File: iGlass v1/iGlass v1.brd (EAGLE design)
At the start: 86.4 x 22.9 mm, 13 parts, among them J1 1040310811, U1 ABX00027

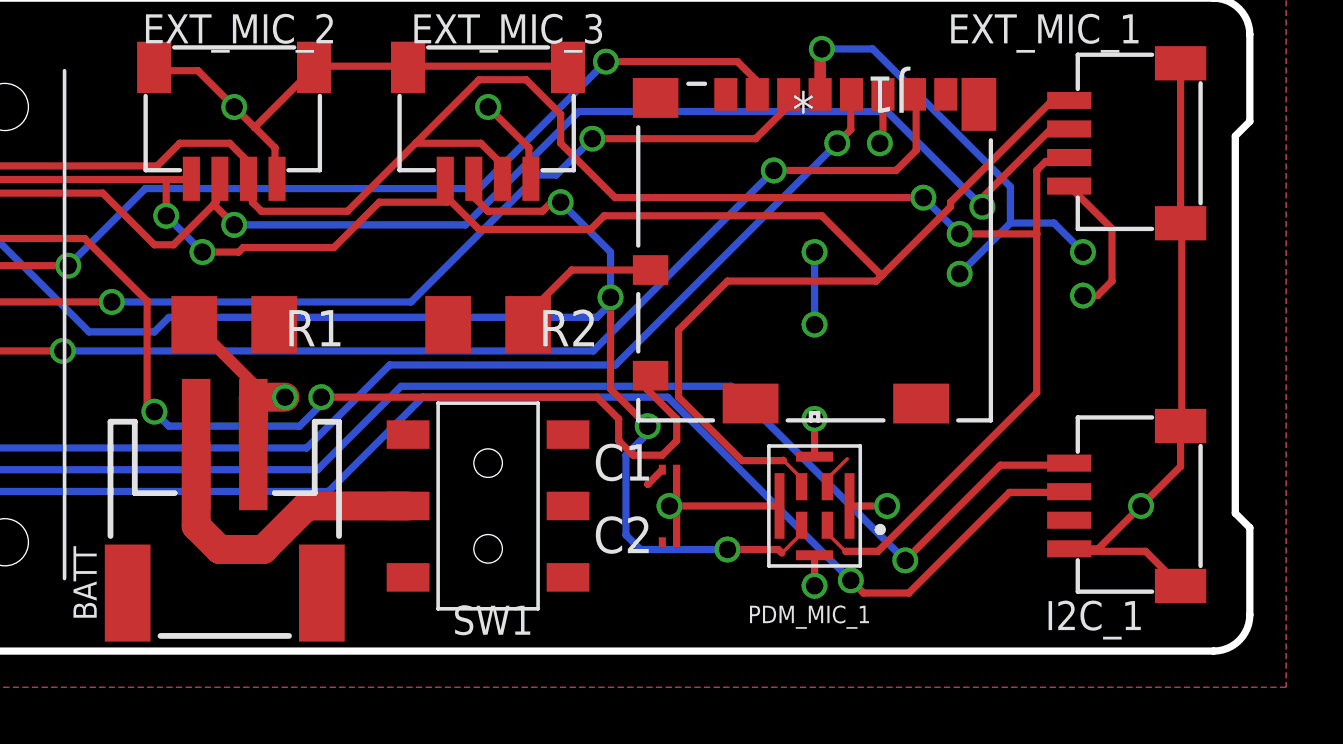
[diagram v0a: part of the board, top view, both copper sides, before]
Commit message: add pcb v2, v3
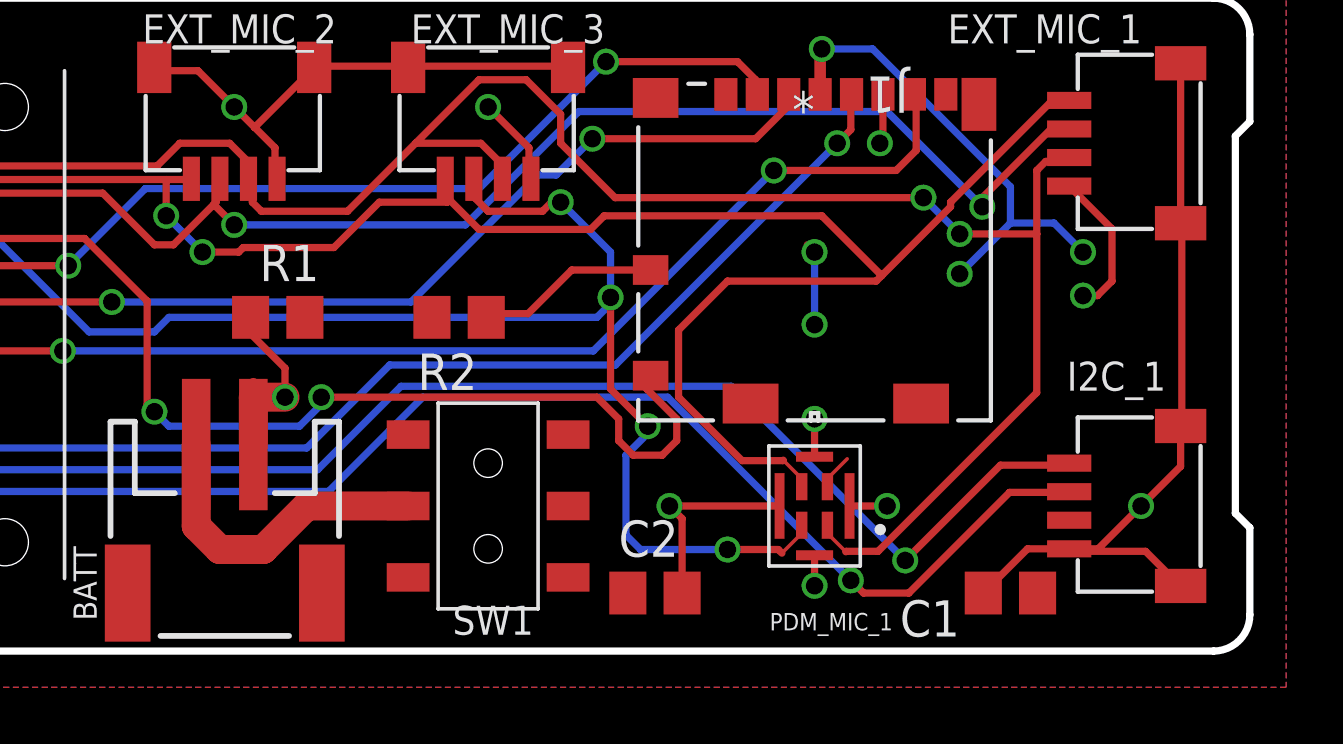
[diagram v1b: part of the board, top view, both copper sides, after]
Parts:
- C1, C2: device rcl:C0201 -> rcl:C0805
- R1, R2: device resistor:M1206 -> resistor:R0805
- moved C1 12.7 mm to (79.5, 3.56), turned to 180 degrees
- moved C2 1.85 mm to (67.1, 3.56)
- moved R1 1.55 mm to (53.8, 13.2)
- moved R2 1.05 mm to (60.2, 13.2), turned to 180 degrees
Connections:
- net N$3: now also R2.1; no longer R2.2
- net VCC: now also R2.2; no longer R2.1
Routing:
- net GND: track 73.4 -> 77.9 mm
- net N$3: track 5.31 -> 6.44 mm
- net VCC: track 21.6 -> 20.9 mm
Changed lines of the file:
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@@
 <attribute name="MF" value="STMicroelectronics" x="72.644" y="6.604" size="1.778" layer="27" rot="R180" display="off"/>
 <attribute name="MP" value="MP34DT01-M" x="72.644" y="6.604" size="1.778" layer="27" rot="R180" display="off"/>
-<attribute name="NAME" x="74.620390625" y="3.111240625" size="0.6096" layer="25" rot="R180"/>
+<attribute name="NAME" x="75.382390625" y="2.857240625" size="0.6096" layer="25" rot="R180"/>
 <attribute name="PACKAGE" value="None" x="72.644" y="6.604" size="1.778" layer="27" rot="R180" display="off"/>
 <attribute name="PRICE" value="None" x="72.644" y="6.604" size="1.778" layer="27" rot="R180" display="off"/>
@@
 <attribute name="PURCHASE-URL" value="https://pricing.snapeda.com/search/part/ABX00027/?ref=eda" x="24.384" y="12.954" size="1.778" layer="27" display="off"/>
 </element>
-<element name="C1" library="rcl" package="C0201" value="10uF" x="67.564" y="7.874" smashed="yes">
-<attribute name="NAME" x="64.897" y="7.493" size="1.27" layer="25"/>
-<attribute name="VALUE" x="67.183" y="8.255" size="1.27" layer="27"/>
-</element>
-<element name="C2" library="rcl" package="C0201" value="0.1uF" x="67.564" y="5.334" smashed="yes">
-<attribute name="NAME" x="64.897" y="4.953" size="1.27" layer="25"/>
-<attribute name="VALUE" x="65.405" y="3.175" size="1.27" layer="27"/>
-</element>
-<element name="R1" library="resistor" package="M1206" value="10K" x="52.324" y="12.954" smashed="yes">
-<attribute name="NAME" x="54.102" y="12.192" size="1.27" layer="25"/>
-<attribute name="VALUE" x="54.102" y="13.97" size="1.27" layer="27"/>
-</element>
 <element name="J1" library="micro_sd_slot" package="104031-0811_MOL" value="1040310811" x="72.644" y="15.494" smashed="yes" rot="R180">
 <attribute name="COPYRIGHT" value="Copyright (C) 2021 Ultra Librarian. All rights reserved." x="72.644" y="15.494" size="1.778" layer="27" rot="R180" display="off"/>
@@
 <attribute name="VALUE" x="74.3712" y="21.6408" size="1.27" layer="27" ratio="6" rot="SR180"/>
 </element>
-<element name="R2" library="resistor" package="M1206" value="100K" x="61.214" y="12.954" smashed="yes">
-<attribute name="NAME" x="62.992" y="12.192" size="1.27" layer="25"/>
-<attribute name="VALUE" x="60.96" y="14.224" size="1.27" layer="27"/>
-</element>
 <element name="EXT_MIC_3" library="smart-glasses" package="MICROBUILDER_JST_SH4" value="MICROBUILDER_STEMMA_I2C_QT" x="61.214" y="20.574" smashed="yes" rot="R180">
 <attribute name="NAME" x="65.306" y="23.818" size="1.016" layer="25" rot="R180"/>
 </element>
 <element name="I2C_1" library="smart-glasses" package="MICROBUILDER_JST_SH4" value="MICROBUILDER_STEMMA_I2C_QT" x="84.074" y="6.604" smashed="yes" rot="R90">
-<attribute name="NAME" x="80.714" y="2.258" size="1.016" layer="25"/>
+<attribute name="NAME" x="81.476" y="10.64" size="1.016" layer="25"/>
 </element>
 <element name="EXT_MIC_2" library="smart-glasses" package="MICROBUILDER_JST_SH4" value="MICROBUILDER_STEMMA_I2C_QT" x="52.324" y="20.574" smashed="yes" rot="R180">
@@
 <attribute name="NAME" x="46.6979" y="5.1943" size="0.8128" layer="25" ratio="18" rot="R270"/>
 <attribute name="VALUE" x="54.2163" y="3.7846" size="0.4064" layer="27" ratio="10" rot="R180"/>
+</element>
+<element name="R2" library="resistor" package="R0805" value="100K" x="60.198" y="13.208" smashed="yes" rot="R180">
+<attribute name="NAME" x="60.833" y="11.938" size="1.27" layer="25" rot="R180"/>
+<attribute name="VALUE" x="60.833" y="15.748" size="1.27" layer="27" rot="R180"/>
+</element>
+<element name="R1" library="resistor" package="R0805" value="10K" x="53.848" y="13.208" smashed="yes">
+<attribute name="NAME" x="53.213" y="14.478" size="1.27" layer="25"/>
+<attribute name="VALUE" x="53.213" y="10.668" size="1.27" layer="27"/>
+</element>
+<element name="C1" library="rcl" package="C0805" value="10uF" x="79.502" y="3.556" smashed="yes" rot="R180">
+<attribute name="NAME" x="77.724" y="3.302" size="1.27" layer="25" rot="R180"/>
+<attribute name="VALUE" x="80.772" y="6.096" size="1.27" layer="27" rot="R180"/>
+</element>
+<element name="C2" library="rcl" package="C0805" value="0.1uF" x="67.056" y="3.556" smashed="yes">
+<attribute name="NAME" x="65.786" y="4.826" size="1.27" layer="25"/>
+<attribute name="VALUE" x="70.104" y="2.032" size="1.27" layer="27" rot="R90"/>
 </element>
 </elements>
@@
 <contactref element="PDM_MIC_1" pad="5_3"/>
 <contactref element="PDM_MIC_1" pad="5_4"/>
-<contactref element="C2" pad="2"/>
-<contactref element="C1" pad="2"/>
-<contactref element="R1" pad="1"/>
 <contactref element="J1" pad="6"/>
 <contactref element="EXT_MIC_2" pad="MT1"/>
@@
 <wire x1="71.419" y1="6.604" x2="67.564" y2="6.604" width="0.254" layer="1"/>
 <via x="67.564" y="6.604" extent="1-16" drill="0.6096"/>
-<wire x1="67.814" y1="7.874" x2="67.814" y2="6.854" width="0.254" layer="1"/>
-<wire x1="67.814" y1="6.854" x2="67.564" y2="6.604" width="0.254" layer="1"/>
-<wire x1="67.814" y1="5.334" x2="67.814" y2="6.354" width="0.254" layer="1"/>
-<wire x1="67.814" y1="6.354" x2="67.564" y2="6.604" width="0.254" layer="1"/>
 <polygon width="0.4064" layer="16">
 <vertex x="0.254" y="25.654"/>
@@
 <wire x1="52.9938" y1="10.414" x2="54.102" y2="10.414" width="1.016" layer="1"/>
 <via x="54.102" y="10.414" extent="1-16" drill="0.6096"/>
-<wire x1="50.924" y1="12.954" x2="52.9938" y2="10.8842" width="0.4064" layer="1"/>
 <wire x1="52.9938" y1="10.8842" x2="52.9938" y2="10.414" width="0.4064" layer="1"/>
+<contactref element="R1" pad="1"/>
+<contactref element="C1" pad="2"/>
+<contactref element="C2" pad="2"/>
+<wire x1="68.006" y1="3.556" x2="68.006" y2="6.162" width="0.254" layer="1"/>
+<wire x1="68.006" y1="6.162" x2="67.564" y2="6.604" width="0.254" layer="1"/>
+<wire x1="52.898" y1="13.208" x2="52.898" y2="12.634" width="0.254" layer="1"/>
+<wire x1="52.898" y1="12.634" x2="54.102" y2="11.43" width="0.254" layer="1"/>
+<wire x1="54.102" y1="11.43" x2="54.102" y2="10.414" width="0.254" layer="1"/>
+<wire x1="78.552" y1="3.556" x2="80.1" y2="5.104" width="0.254" layer="1"/>
+<wire x1="80.1" y1="5.104" x2="81.56" y2="5.104" width="0.254" layer="1"/>
 </signal>
 <signal name="VCC">
-<contactref element="C1" pad="1"/>
-<contactref element="C2" pad="1"/>
 <contactref element="PDM_MIC_1" pad="2"/>
-<contactref element="R1" pad="2"/>
 <contactref element="J1" pad="4"/>
-<contactref element="R2" pad="1"/>
 <contactref element="I2C_1" pad="2"/>
 <contactref element="U1" pad="2"/>
@@
 <wire x1="81.026" y1="16.51" x2="82.042" y2="15.494" width="0.254" layer="16"/>
 <via x="82.042" y="15.494" extent="1-16" drill="0.6096"/>
-<wire x1="67.314" y1="7.874" x2="66.806" y2="7.366" width="0.254" layer="1"/>
-<wire x1="66.806" y1="7.366" x2="66.802" y2="7.366" width="0.254" layer="1"/>
 <wire x1="72.39" y1="15.748" x2="72.644" y2="15.494" width="0.254" layer="1"/>
 <via x="72.644" y="15.494" extent="1-16" drill="0.6096"/>
 <wire x1="72.644" y1="15.494" x2="72.644" y2="12.954" width="0.254" layer="16"/>
 <via x="72.644" y="12.954" extent="1-16" drill="0.6096"/>
+<contactref element="R2" pad="2"/>
+<contactref element="R1" pad="2"/>
+<contactref element="C1" pad="1"/>
+<contactref element="C2" pad="1"/>
 </signal>
 <signal name="PDM_DATA">
@@
 <wire x1="52.959" y1="17.24025" x2="53.2765" y2="16.92275" width="0.254" layer="1"/>
 <wire x1="52.959" y1="18.034" x2="52.824" y2="18.06" width="0.254" layer="1"/>
-<wire x1="61.69025" y1="18.19275" x2="61.714" y2="18.06" width="0.254" layer="1"/>
 <wire x1="21.5265" y1="20.73275" x2="21.5265" y2="22.00275" width="0.254" layer="1"/>
 <wire x1="23.749" y1="18.51025" x2="21.5265" y2="20.73275" width="0.254" layer="1"/>
@@
 <signal name="N$3">
 <contactref element="J1" pad="9"/>
-<contactref element="R2" pad="2"/>
-<wire x1="62.614" y1="12.954" x2="62.614" y2="13.338" width="0.254" layer="1"/>
 <wire x1="62.614" y1="13.338" x2="64.1415" y2="14.8655" width="0.254" layer="1"/>
 <wire x1="64.1415" y1="14.8655" x2="66.904" y2="14.8655" width="0.254" layer="1"/>
+<contactref element="R2" pad="1"/>
+<wire x1="61.148" y1="13.208" x2="61.278" y2="13.338" width="0.254" layer="1"/>
+<wire x1="61.278" y1="13.338" x2="62.614" y2="13.338" width="0.254" layer="1"/>
 </signal>
 <signal name="SDA">
